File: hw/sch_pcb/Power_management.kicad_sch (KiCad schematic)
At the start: 25 parts

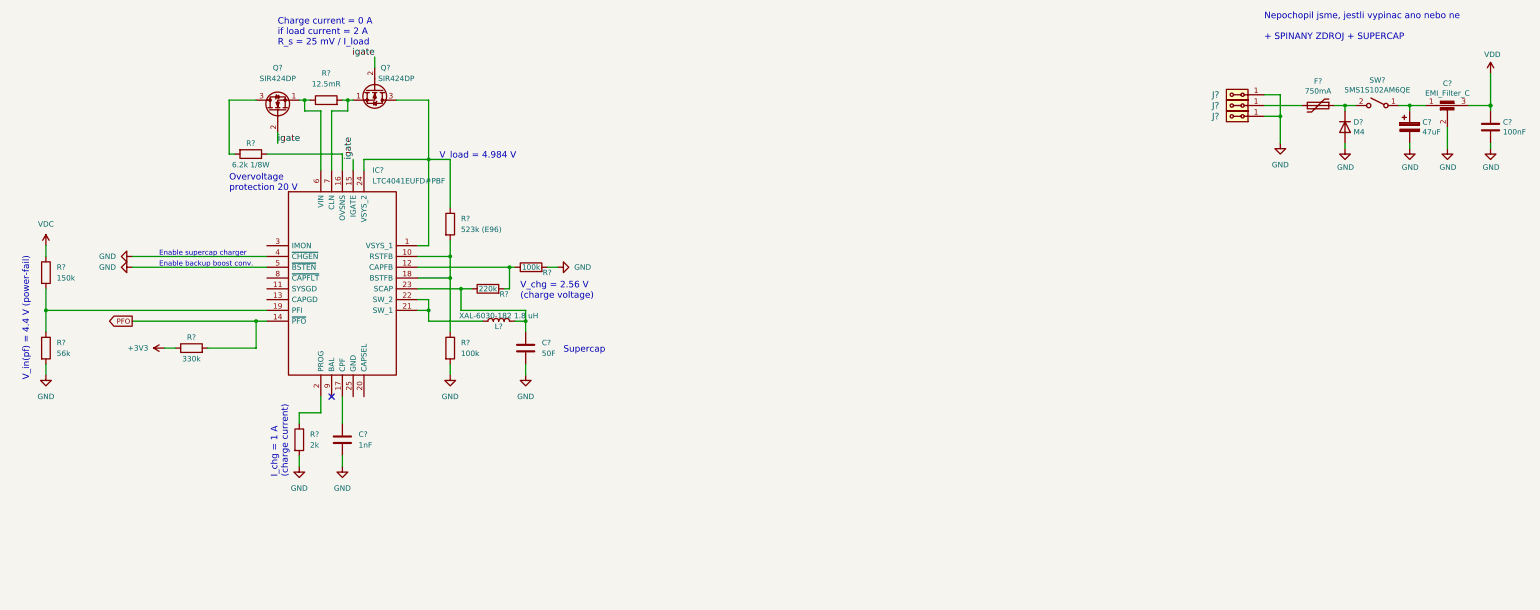
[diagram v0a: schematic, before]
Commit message: schematics update - LTC4041, TPS631000
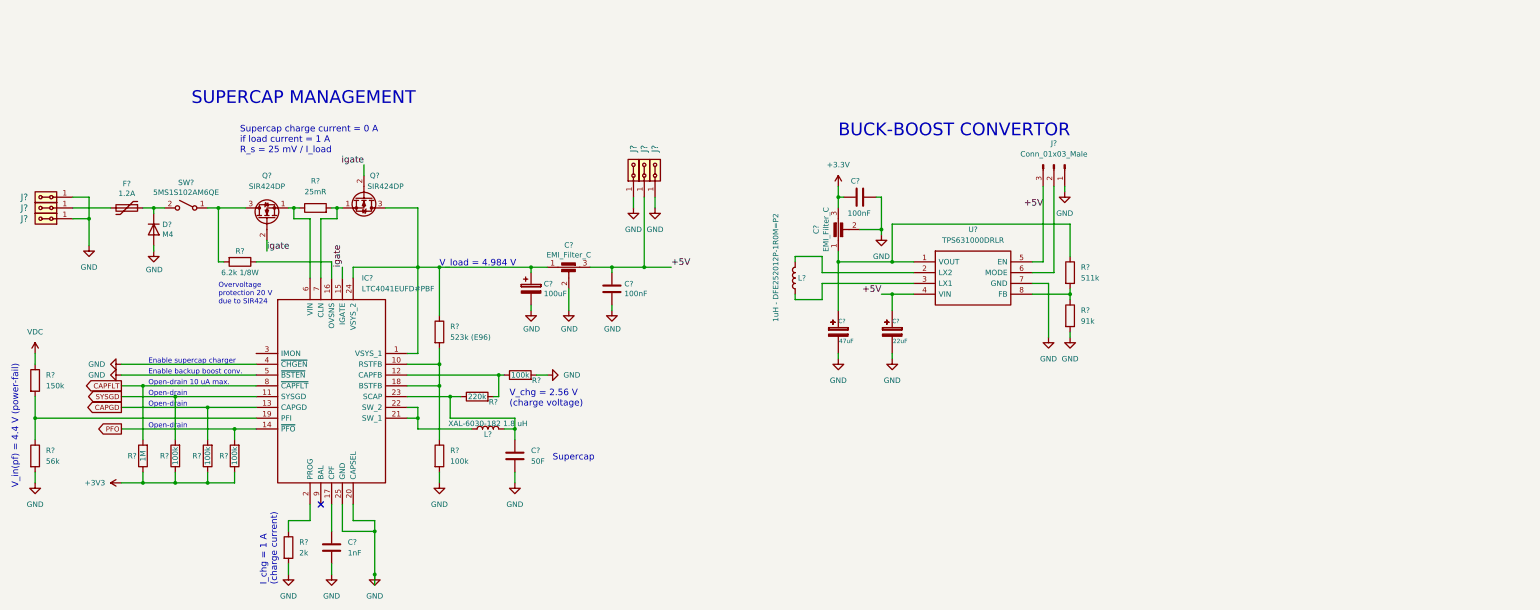
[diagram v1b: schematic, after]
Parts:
- removed C?: EMI_Filter_C, Mlab_L:FIR1, symbol DATALOGGER01A-rescue:EMI_Filter_C-device
- removed C?: 47uF, Mlab_C:TantalC_SizeC_Reflow, symbol DATALOGGER01A-rescue:CP-device
- removed C?: 100nF, Mlab_R:SMD-0805, symbol DATALOGGER01A-rescue:C-device
- added C? (x2): EMI_Filter_C, Mlab_L:FIR1, symbol DATALOGGER01A-rescue:EMI_Filter_C-device
- added C?: 22uF, Mlab_C:TantalC_SizeB_Reflow, symbol LION2CELL01D-rescue:CP2
- added C?: 100uF, Mlab_C:TantalC_SizeC_Reflow, symbol DATALOGGER01A-rescue:CP-device
- added C? (x2): 100nF, Mlab_R:SMD-0805, symbol DATALOGGER01A-rescue:C-device
- added C?: 47uF, Mlab_C:TantalC_SizeB_Reflow, symbol LION2CELL01D-rescue:CP2
- added J? (x3): HEADER_2x01_PARALLEL, Mlab_Pin_Headers:Straight_2x01, symbol DATALOGGER01A-rescue:HEADER_2x01_PARALLEL-MLAB_HEADER
- added J?: Conn_01x03_Male, symbol Connector:Conn_01x03_Male
- added L?: 1uH - DFE252012P-1R0M=P2, symbol Device:L
- added R? (x2): 100k, symbol Device:R
- added R?: 1M, symbol Device:R
- added R?: 91k, symbol Device:R
- added R?: 511k, symbol Device:R
- added U?: TPS631000DRLR, SOTFL50P160X60-8N, symbol TPS631000DRLR:TPS631000DRLR
- F?: value 750mA -> 1.2A
- R?: value 330k -> 100k
- R?: value 12.5mR -> 25mR
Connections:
- net +3V3: now also R?.1, R?.1, R?.1
- net GND: now also IC?.20 (CAPSEL), IC?.25 (GND), C?.2, C?.2, C?.2, C?.2, C?.2, C?.2, C?.2, J?.1, J?.1, J?.1 (Pin_1), J?.2, J?.2, R?.2, U?.7 (GND)
- net at Q?.3 (D), R?.2: now also SW?.1 (A)
- net at IC?.1 (VSYS_1), IC?.24 (VSYS_2), Q?.3 (D)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: now also C?.1, C?.1
- net SYSGD: now reaches IC?.11 (SYSGD)
- net SYSGD: now also R?.2
- net CAPGD: now reaches IC?.13 (CAPGD)
- net CAPGD: now also R?.2
- net CAPFLT: now reaches IC?.8 (~{CAPFLT})
- net CAPFLT: now also R?.2
- new net: R?.1, R?.2, U?.8 (FB)
- new net: C?.1, C?.1, R?.1, U?.1 (VOUT)
- new net: L?.2, U?.2 (LX2)
- new net: L?.1, U?.3 (LX1)
- new net: J?.2 (Pin_2), U?.6 (MODE)
- new net +3.3V: C?.1, C?.3
- new net +5V: C?.1, C?.1, C?.3, J?.1, J?.2, J?.3 (Pin_3), U?.4 (VIN), U?.5 (EN)
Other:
- note added: "BUCK-BOOST CONVERTOR"
- note added: "Open-drain"
- note added: "Open-drain 10 uA max."
- note added: "Overvoltage protection 20 V due to SIR424"
- note added: "SUPERCAP MANAGEMENT"
- note added: "Supercap charge current = 0 A if load current = 1 A R_s = 25 mV / I_load"
- note removed: "Charge current = 0 A if load current = 2 A R_s = 25 mV / I_load"
- note removed: "Nepochopil jsme, jestli vypinac ano nebo ne + SPINANY ZDROJ + SUPERCAP"
- note removed: "Overvoltage protection 20 V"
- moved on the sheet: C?, D?, F?, IC?, J?, L?, Q?, R?, SW?
